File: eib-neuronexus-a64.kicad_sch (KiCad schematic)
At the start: 4 parts, among them J1 xOLC-110-01-S-Q_1, J2 xOLC-110-01-S-Q_1, J3 Conn_02x35_Odd_Even, J4 Conn_01x02_Male

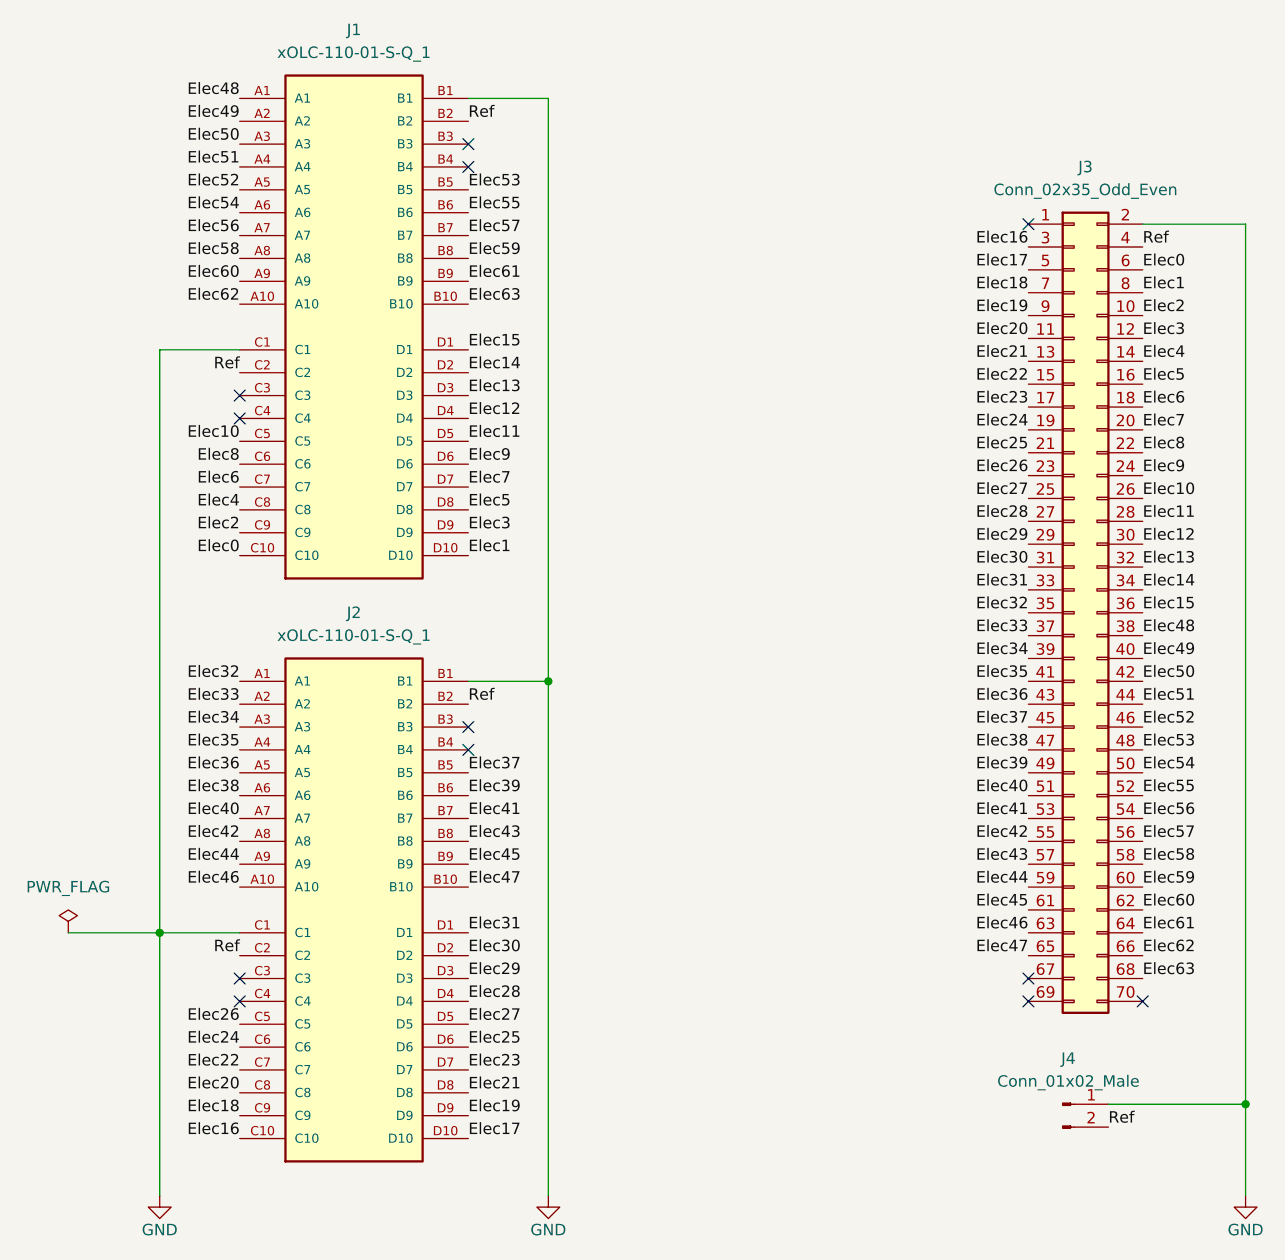
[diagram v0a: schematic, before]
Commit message: Updated with alternative SMD package for big 5x8 connector
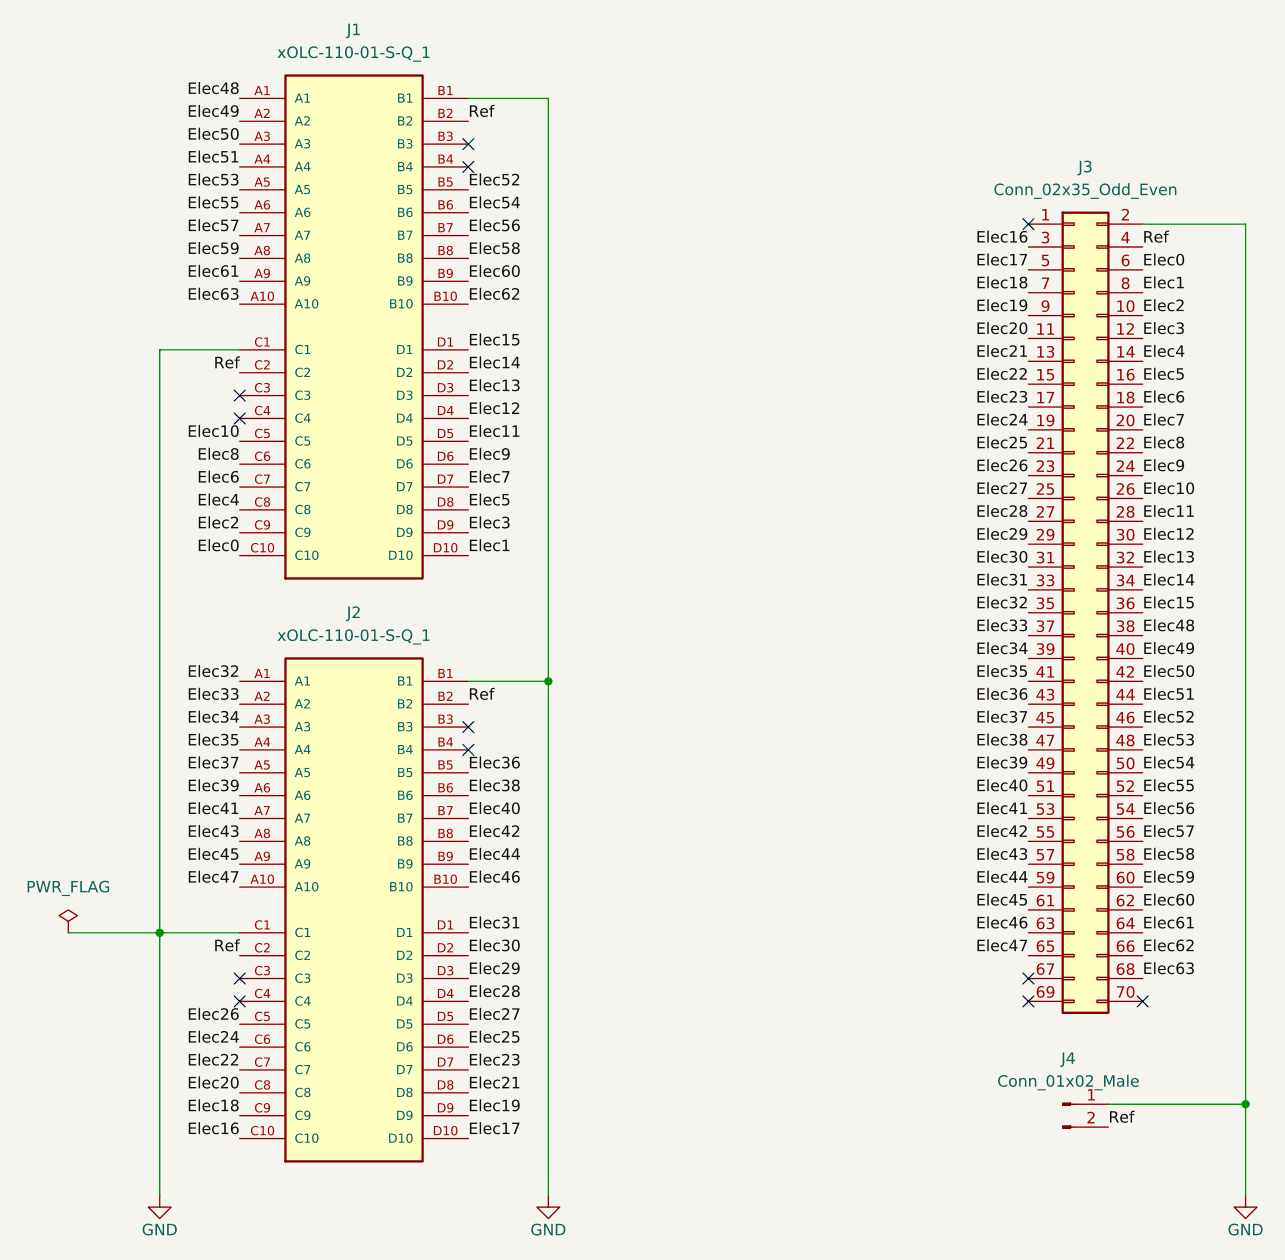
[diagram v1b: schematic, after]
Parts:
- J1, J2: footprint jonnew:SAMTEC_FOLC-110-01-S-Q -> FOLC:SAMTEC_FOLC-110-02-S-Q-LC
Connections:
- net Elec36: now also J2.B5; no longer J2.A5
- net Elec37: now also J2.A5; no longer J2.B5
- net Elec38: now also J2.B6; no longer J2.A6
- net Elec39: now also J2.A6; no longer J2.B6
- net Elec40: now also J2.B7; no longer J2.A7
- net Elec41: now also J2.A7; no longer J2.B7
- net Elec42: now also J2.B8; no longer J2.A8
- net Elec43: now also J2.A8; no longer J2.B8
- net Elec44: now also J2.B9; no longer J2.A9
- net Elec45: now also J2.A9; no longer J2.B9
- net Elec46: now also J2.B10; no longer J2.A10
- net Elec47: now also J2.A10; no longer J2.B10
- net Elec52: now also J1.B5; no longer J1.A5
- net Elec53: now also J1.A5; no longer J1.B5
- net Elec54: now also J1.B6; no longer J1.A6
- net Elec55: now also J1.A6; no longer J1.B6
- net Elec56: now also J1.B7; no longer J1.A7
- net Elec57: now also J1.A7; no longer J1.B7
- net Elec58: now also J1.B8; no longer J1.A8
- net Elec59: now also J1.A8; no longer J1.B8
- net Elec60: now also J1.B9; no longer J1.A9
- net Elec61: now also J1.A9; no longer J1.B9
- net Elec62: now also J1.B10; no longer J1.A10
- net Elec63: now also J1.A10; no longer J1.B10
